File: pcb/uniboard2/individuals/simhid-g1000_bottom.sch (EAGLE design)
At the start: 29 parts, among them J2 PCB-INTERCONNECT, J3 PCB-INTERCONNECT, SW15 TS-1109S-B-B, SW16 TS-1109S-B-B, SW17 TS-1109S-B-B, SW18 TS-1109S-B-B, SW19 TS-1109S-B-B, SW20 TS-1109S-B-B, SW21 TS-1109S-B-B, SW22 TS-1109S-B-B, SW23 TS-1109S-B-B, SW24 TS-1109S-B-B, SW25 TS-1109S-B-B, SW26 TS-1109S-B-B, U3 MCP23S17-E

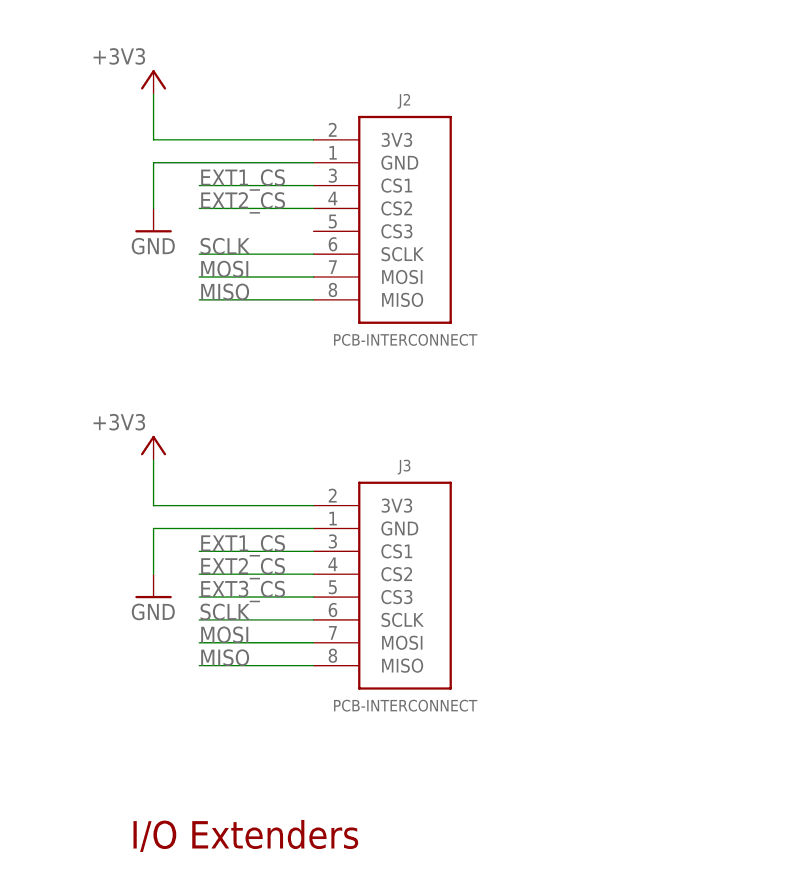
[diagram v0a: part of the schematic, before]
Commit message: Added vertical USB connector versions
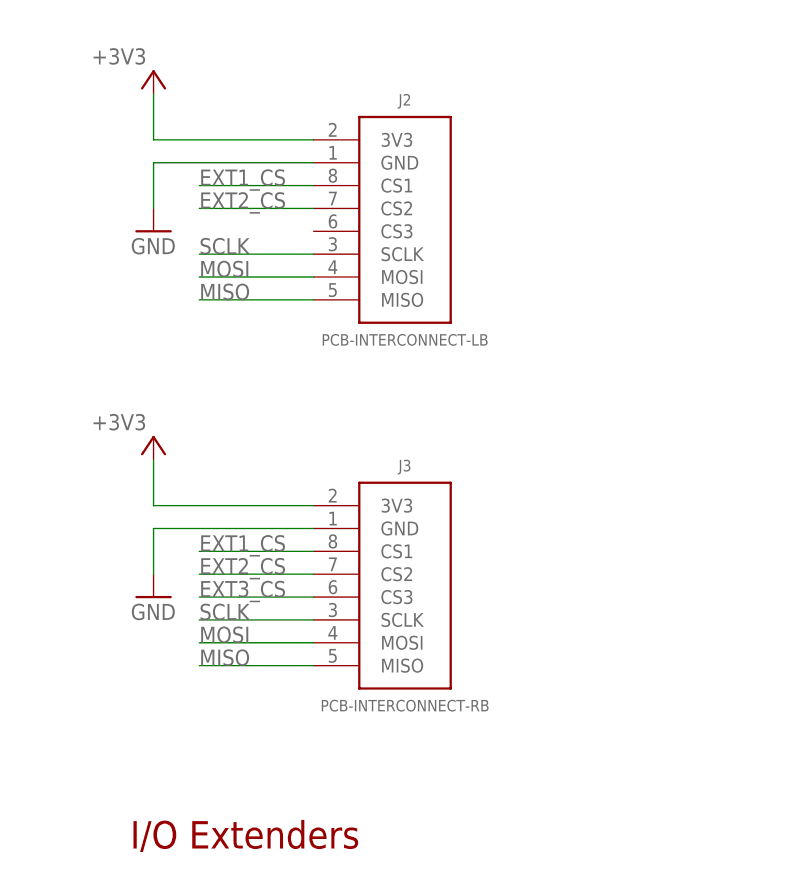
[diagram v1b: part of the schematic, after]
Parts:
- J2: value PCB-INTERCONNECT -> PCB-INTERCONNECT-LB; device SimHID-G1000:PCB-INTERCONNECT -> SimHID-G1000:PCB-INTERCONNECT-LB
- J3: value PCB-INTERCONNECT -> PCB-INTERCONNECT-RB; device SimHID-G1000:PCB-INTERCONNECT -> SimHID-G1000:PCB-INTERCONNECT-RB
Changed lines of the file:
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@@
 </classes>
 <parts>
-<part name="J2" library="SimHID-G1000" library_urn="urn:adsk.eagle:library:27646014" deviceset="PCB-INTERCONNECT" device="" package3d_urn="urn:adsk.eagle:package:27646017/2"/>
+<part name="J2" library="SimHID-G1000" library_urn="urn:adsk.eagle:library:27646014" deviceset="PCB-INTERCONNECT" device="-LB" package3d_urn="urn:adsk.eagle:package:41622066/4" value="PCB-INTERCONNECT-LB"/>
 <part name="+3V2" library="supply1" library_urn="urn:adsk.eagle:library:371" deviceset="+3V3" device=""/>
 <part name="GND3" library="supply1" library_urn="urn:adsk.eagle:library:371" deviceset="GND" device=""/>
@@
 <part name="R11" library="gen-discrete3" library_urn="urn:adsk.eagle:library:8961849" deviceset="RCL_R-US_" device="R0402-HS" package3d_urn="urn:adsk.eagle:package:8961860/5" value="10KΩ"/>
 <part name="GND4" library="supply1" library_urn="urn:adsk.eagle:library:371" deviceset="GND" device=""/>
-<part name="J3" library="SimHID-G1000" library_urn="urn:adsk.eagle:library:27646014" deviceset="PCB-INTERCONNECT" device="" package3d_urn="urn:adsk.eagle:package:27646017/2"/>
+<part name="J3" library="SimHID-G1000" library_urn="urn:adsk.eagle:library:27646014" deviceset="PCB-INTERCONNECT" device="-RB" package3d_urn="urn:adsk.eagle:package:41620115/5" value="PCB-INTERCONNECT-RB"/>
 <part name="+3V3" library="supply1" library_urn="urn:adsk.eagle:library:371" deviceset="+3V3" device=""/>
 <part name="GND2" library="supply1" library_urn="urn:adsk.eagle:library:371" deviceset="GND" device=""/>
